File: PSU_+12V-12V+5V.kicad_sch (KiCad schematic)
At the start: 41 parts, among them J1 PSU12a, J2 PSU12b, Q1 BC557, Q2 BC557, Q3 BC547, Q4 BC547, U1 LM317L, U2 LM317L

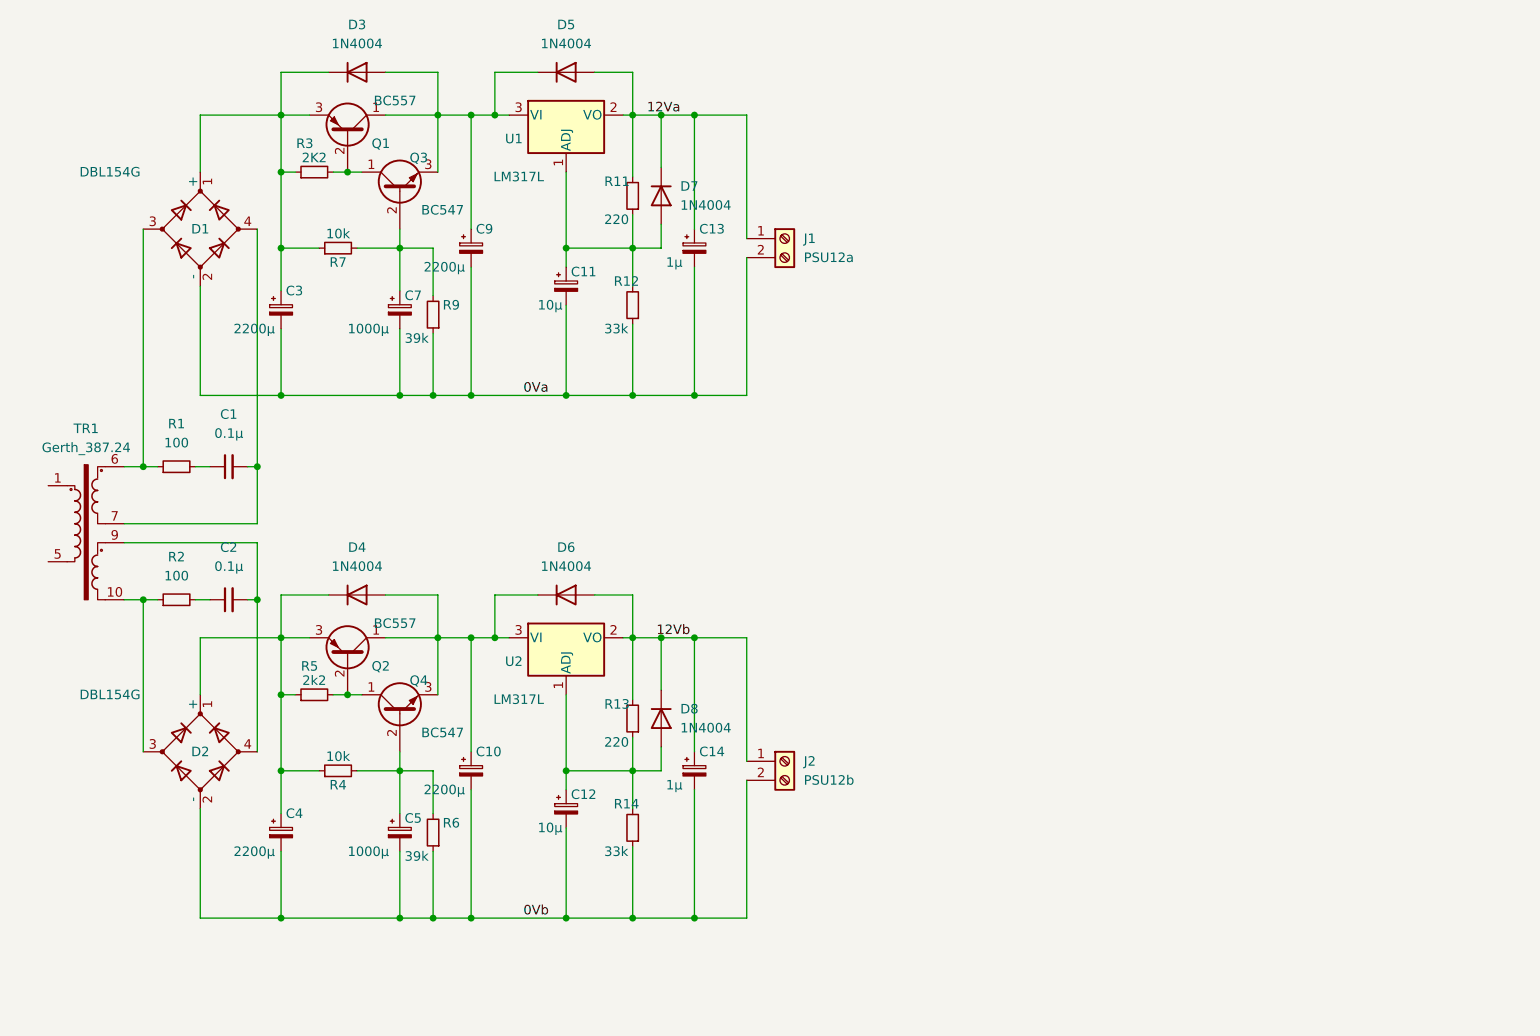
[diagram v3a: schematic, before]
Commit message: Add 5V part + 230 volt connection
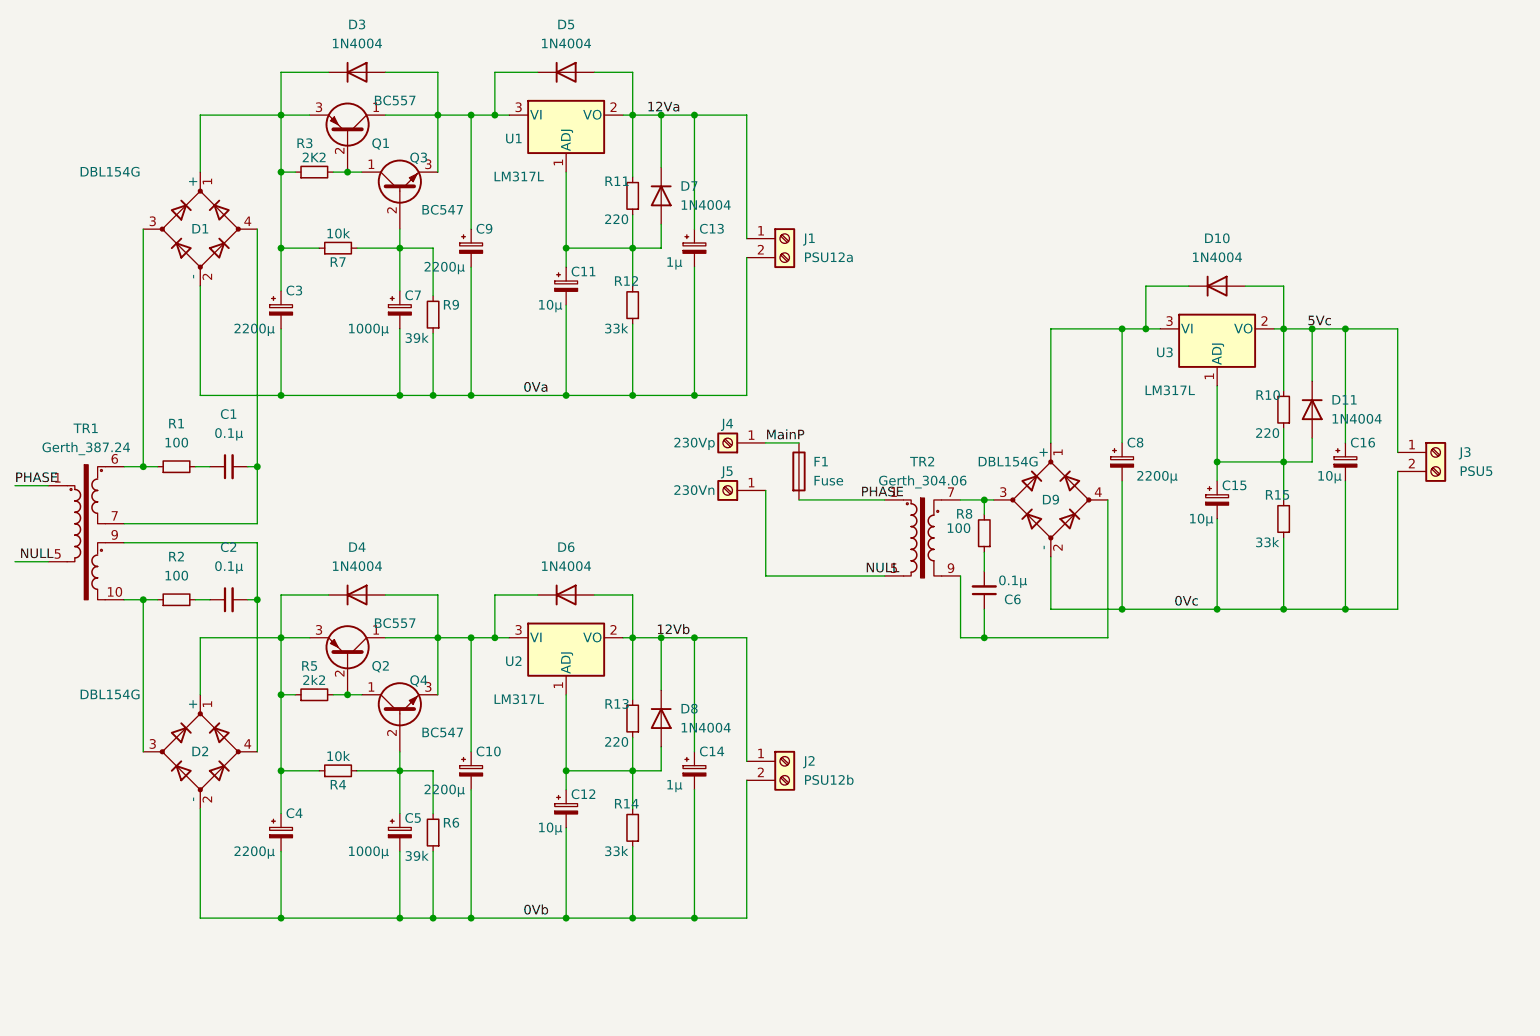
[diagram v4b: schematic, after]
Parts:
- added C15, C16: 10µ, Capacitor_THT:CP_Radial_D5.0mm_P2.50mm, symbol Device:C_Polarized_Small
- added C6: 0.1µ, Capacitor_SMD:C_1206_3216Metric_Pad1.33x1.80mm_HandSolder, symbol Device:C_Small
- added C8: 2200µ, Capacitor_THT:CP_Radial_D16.0mm_P7.50mm, symbol Device:C_Polarized_Small
- added D10, D11: 1N4004, Diode_THT:D_DO-41_SOD81_P10.16mm_Horizontal, symbol Diode:1N4004
- added D9: DBL154G, MyFootPrints:DBL_4, symbol Device:D_Bridge_+-AA
- added F1: Fuse, MyFootPrints:Fuse_Littelfuse-PTF15, symbol Device:Fuse
- added J3: PSU5, TerminalBlock_Phoenix:TerminalBlock_Phoenix_MKDS-1,5-2_1x02_P5.00mm_Horizontal, symbol Connector:Screw_Terminal_01x02
- added J4: 230Vp, TerminalBlock_MetzConnect:TerminalBlock_MetzConnect_360271_1x01_Horizontal_ScrewM3.0_Boxed, symbol Connector:Screw_Terminal_01x01
- added J5: 230Vn, TerminalBlock_MetzConnect:TerminalBlock_MetzConnect_360271_1x01_Horizontal_ScrewM3.0_Boxed, symbol Connector:Screw_Terminal_01x01
- added R10: 220, Resistor_SMD:R_1206_3216Metric_Pad1.30x1.75mm_HandSolder, symbol Device:R_Small
- added R15: 33k, Resistor_SMD:R_1206_3216Metric_Pad1.30x1.75mm_HandSolder, symbol Device:R_Small
- added R8: 100, Resistor_SMD:R_1206_3216Metric_Pad1.30x1.75mm_HandSolder, symbol Device:R_Small
- added TR2: Gerth_304.06, MyFootPrints:304.06_1.8VA, symbol Transformer:TEZ1.5-D-1
- added U3: LM317L, Package_TO_SOT_THT:TO-92_Inline_Wide, symbol Regulator_Linear:LM317L_TO92
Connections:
- net PHASE: now reaches TR1.1
- net PHASE: now also F1.2, TR2.1
- net NULL: now reaches TR1.5
- net NULL: now also J5.1 (Pin_1), TR2.5
- new net: C6.2, R8.1
- new net: D9.3, R8.2, TR2.7
- new net: C15.1, D11.2 (A), R10.1, R15.2, U3.1 (ADJ)
- new net: C8.1, D10.1 (K), D9.1 (+), U3.3 (VI)
- new net: C6.1, D9.4, TR2.9
- new net 0Vc: C15.2, C16.2, C8.2, D9.2 (-), J3.2 (Pin_2), R15.1
- new net 5Vc: C16.1, D10.2 (A), D11.1 (K), J3.1 (Pin_1), R10.2, U3.2 (VO)
- new net MainP: F1.1, J4.1 (Pin_1)

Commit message: ...
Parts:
- removed J4: 230Vp, TerminalBlock_MetzConnect:TerminalBlock_MetzConnect_360271_1x01_Horizontal_ScrewM3.0_Boxed, symbol Connector:Screw_Terminal_01x01
- removed J5: 230Vn, TerminalBlock_MetzConnect:TerminalBlock_MetzConnect_360271_1x01_Horizontal_ScrewM3.0_Boxed, symbol Connector:Screw_Terminal_01x01
- added H1, H2, H3, H4: MountingHole, MountingHole:MountingHole_3.2mm_M3, symbol Mechanical:MountingHole
- added J4: 230V, TerminalBlock_Phoenix:TerminalBlock_Phoenix_MKDS-1,5-3_1x03_P5.00mm_Horizontal, symbol Connector:Screw_Terminal_01x03
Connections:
- net MainP: now also J4.3 (Pin_3)
- net NULL: now also J4.1 (Pin_1)
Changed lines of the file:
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@@
     (stroke (width 0) (type default) (color 0 0 0 0))
   )
-  (wire (pts (xy 120.65 77.47) (xy 120.65 88.9))
+  (wire (pts (xy 120.65 76.2) (xy 120.65 88.9))
     (stroke (width 0) (type default) (color 0 0 0 0))
   )
@@
     (stroke (width 0) (type default) (color 0 0 0 0))
   )
+  (wire (pts (xy 118.11 76.2) (xy 120.65 76.2))
+    (stroke (width 0) (type default) (color 0 0 0 0))
+  )
   (wire (pts (xy 180.975 81.28) (xy 180.975 93.345))
     (stroke (width 0) (type default) (color 0 0 0 0))
@@
     (stroke (width 0) (type default) (color 0 0 0 0))
   )
-  (wire (pts (xy 120.65 71.12) (xy 125.095 71.12))
+  (wire (pts (xy 118.11 71.12) (xy 125.095 71.12))
     (stroke (width 0) (type default) (color 0 0 0 0))
   )
@@
     (pin "2")
   )
+  (symbol (lib_id "Mechanical:MountingHole") (at 154.9683 21.6637 0) (unit 1)
+    (in_bom yes) (on_board yes) (fields_autoplaced)
+    (property "Reference" "H2" (id 0) (at 157.5083 20.3936 0)
+      (effects (font (size 1.27 1.27)) (justify left))
+    )
+    (property "Value" "MountingHole" (id 1) (at 157.5083 22.9336 0)
+      (effects (font (size 1.27 1.27)) (justify left))
+    )
+    (property "Footprint" "MountingHole:MountingHole_3.2mm_M3" (id 2) (at 154.9683 21.6637 0)
+      (effects (font (size 1.27 1.27)) hide)
+    )
+    (property "Datasheet" "~" (id 3) (at 154.9683 21.6637 0)
+      (effects (font (size 1.27 1.27)) hide)
+    )
+  )
   (symbol (lib_id "Diode:1N4004") (at 106.68 107.95 270) (unit 1)
     (in_bom yes) (on_board yes) (fields_autoplaced)
@@
     (pin "1")
     (pin "2")
+  )
+  (symbol (lib_id "Mechanical:MountingHole") (at 161.29 21.59 0) (unit 1)
+    (in_bom yes) (on_board yes) (fields_autoplaced)
+    (property "Reference" "H1" (id 0) (at 163.83 20.3199 0)
+      (effects (font (size 1.27 1.27)) (justify left))
+    )
+    (property "Value" "MountingHole" (id 1) (at 163.83 22.8599 0)
+      (effects (font (size 1.27 1.27)) (justify left))
+    )
+    (property "Footprint" "MountingHole:MountingHole_3.2mm_M3" (id 2) (at 161.29 21.59 0)
+      (effects (font (size 1.27 1.27)) hide)
+    )
+    (property "Datasheet" "~" (id 3) (at 161.29 21.59 0)
+      (effects (font (size 1.27 1.27)) hide)
+    )
   )
   (symbol (lib_id "Diode:1N4004") (at 193.675 66.675 270) (unit 1)
@@
     (pin "2")
   )
-  (symbol (lib_id "Connector:Screw_Terminal_01x01") (at 115.57 77.47 180) (unit 1)
-    (in_bom yes) (on_board yes)
-    (property "Reference" "J5" (id 0) (at 115.57 74.93 0))
-    (property "Value" "230Vn" (id 1) (at 111.125 77.47 0))
-    (property "Footprint" "TerminalBlock_MetzConnect:TerminalBlock_MetzConnect_360271_1x01_Horizontal_ScrewM3.0_Boxed" (id 2) (at 115.57 77.47 0)
-      (effects (font (size 1.27 1.27)) hide)
-    )
-    (property "Datasheet" "~" (id 3) (at 115.57 77.47 0)
-      (effects (font (size 1.27 1.27)) hide)
-    )
-    (pin "1")
+  (symbol (lib_id "Mechanical:MountingHole") (at 161.7213 28.0636 0) (unit 1)
+    (in_bom yes) (on_board yes) (fields_autoplaced)
+    (property "Reference" "H4" (id 0) (at 164.2613 26.7935 0)
+      (effects (font (size 1.27 1.27)) (justify left))
+    )
+    (property "Value" "MountingHole" (id 1) (at 164.2613 29.3335 0)
+      (effects (font (size 1.27 1.27)) (justify left))
+    )
+    (property "Footprint" "MountingHole:MountingHole_3.2mm_M3" (id 2) (at 161.7213 28.0636 0)
+      (effects (font (size 1.27 1.27)) hide)
+    )
+    (property "Datasheet" "~" (id 3) (at 161.7213 28.0636 0)
+      (effects (font (size 1.27 1.27)) hide)
+    )
   )
   (symbol (lib_id "Device:R_Small") (at 41.91 74.295 90) (unit 1)
@@
     (pin "1")
     (pin "2")
+  )
+  (symbol (lib_id "Mechanical:MountingHole") (at 154.9683 28.4167 0) (unit 1)
+    (in_bom yes) (on_board yes) (fields_autoplaced)
+    (property "Reference" "H3" (id 0) (at 157.5083 27.1466 0)
+      (effects (font (size 1.27 1.27)) (justify left))
+    )
+    (property "Value" "MountingHole" (id 1) (at 157.5083 29.6866 0)
+      (effects (font (size 1.27 1.27)) (justify left))
+    )
+    (property "Footprint" "MountingHole:MountingHole_3.2mm_M3" (id 2) (at 154.9683 28.4167 0)
+      (effects (font (size 1.27 1.27)) hide)
+    )
+    (property "Datasheet" "~" (id 3) (at 154.9683 28.4167 0)
+      (effects (font (size 1.27 1.27)) hide)
+    )
   )
   (symbol (lib_id "Device:C_Small") (at 48.895 92.075 90) (unit 1)
@@
     (pin "3")
   )
-  (symbol (lib_id "Connector:Screw_Terminal_01x01") (at 115.57 71.12 180) (unit 1)
-    (in_bom yes) (on_board yes)
-    (property "Reference" "J4" (id 0) (at 115.57 68.58 0))
-    (property "Value" "230Vp" (id 1) (at 111.125 71.12 0))
-    (property "Footprint" "TerminalBlock_MetzConnect:TerminalBlock_MetzConnect_360271_1x01_Horizontal_ScrewM3.0_Boxed" (id 2) (at 115.57 71.12 0)
-      (effects (font (size 1.27 1.27)) hide)
-    )
-    (property "Datasheet" "~" (id 3) (at 115.57 71.12 0)
-      (effects (font (size 1.27 1.27)) hide)
-    )
-    (pin "1")
-  )
   (symbol (lib_id "Diode:1N4004") (at 93.98 91.44 0) (unit 1)
     (in_bom yes) (on_board yes) (fields_autoplaced)
@@
     (pin "2")
   )
+  (symbol (lib_id "Connector:Screw_Terminal_01x03") (at 113.03 73.66 180) (unit 1)
+    (in_bom yes) (on_board yes)
+    (property "Reference" "J4" (id 0) (at 113.03 64.77 0))
+    (property "Value" "230V" (id 1) (at 108.585 73.66 0))
+    (property "Footprint" "TerminalBlock_Phoenix:TerminalBlock_Phoenix_MKDS-1,5-3_1x03_P5.00mm_Horizontal" (id 2) (at 113.03 73.66 0)
+      (effects (font (size 1.27 1.27)) hide)
+    )
+    (property "Datasheet" "~" (id 3) (at 113.03 73.66 0)
+      (effects (font (size 1.27 1.27)) hide)
+    )
+    (pin "1")
+    (pin "2")
+    (pin "3")
+  )
   (sheet_instances
     (path "/" (page "1"))
@@
       (reference "F1") (unit 1) (value "Fuse") (footprint "MyFootPrints:Fuse_Littelfuse-PTF15")
     )
+    (path "/35391cf2-3cf2-436c-8d27-de8c3bcd7990"
+      (reference "H1") (unit 1) (value "MountingHole") (footprint "MountingHole:MountingHole_3.2mm_M3")
+    )
+    (path "/092f2b1b-cd5d-443d-acd1-a09235859417"
+      (reference "H2") (unit 1) (value "MountingHole") (footprint "MountingHole:MountingHole_3.2mm_M3")
+    )
+    (path "/ae12413a-2d8c-4589-95cf-ebc13663e208"
+      (reference "H3") (unit 1) (value "MountingHole") (footprint "MountingHole:MountingHole_3.2mm_M3")
+    )
+    (path "/56df0299-36cb-4393-9aeb-23633f1a391d"
+      (reference "H4") (unit 1) (value "MountingHole") (footprint "MountingHole:MountingHole_3.2mm_M3")
+    )
     (path "/267aca1d-0cf0-41ab-8780-187b83e1d640"
       (reference "J1") (unit 1) (value "PSU12a") (footprint "TerminalBlock_Phoenix:TerminalBlock_Phoenix_MKDS-1,5-2_1x02_P5.00mm_Horizontal")
@@
       (reference "J3") (unit 1) (value "PSU5") (footprint "TerminalBlock_Phoenix:TerminalBlock_Phoenix_MKDS-1,5-2_1x02_P5.00mm_Horizontal")
     )
-    (path "/d558509b-4fc8-423f-896a-7afa64c91d0c"
-      (reference "J4") (unit 1) (value "230Vp") (footprint "TerminalBlock_MetzConnect:TerminalBlock_MetzConnect_360271_1x01_Horizontal_ScrewM3.0_Boxed")
-    )
-    (path "/5a936882-5081-4041-9286-57b2f9649293"
-      (reference "J5") (unit 1) (value "230Vn") (footprint "TerminalBlock_MetzConnect:TerminalBlock_MetzConnect_360271_1x01_Horizontal_ScrewM3.0_Boxed")
+    (path "/fdb6604f-32f1-404c-8875-abfafd07f43a"
+      (reference "J4") (unit 1) (value "230V") (footprint "TerminalBlock_Phoenix:TerminalBlock_Phoenix_MKDS-1,5-3_1x03_P5.00mm_Horizontal")
     )
     (path "/961e5191-6ef0-485b-8715-bf0eec14a118"

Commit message: Changed footprint of LM317L
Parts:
- U1, U2, U3: footprint Package_TO_SOT_THT:TO-92_Inline_Wide -> MyFootPrints:LM317L_TO92
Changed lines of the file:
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@@
     (property "Reference" "U3" (id 0) (at 173.99 59.055 0))
     (property "Value" "LM317L" (id 1) (at 174.625 64.135 0))
-    (property "Footprint" "Package_TO_SOT_THT:TO-92_Inline_Wide" (id 2) (at 180.975 50.165 0)
+    (property "Footprint" "MyFootPrints:LM317L_TO92" (id 2) (at 180.975 50.165 0)
       (effects (font (size 1.27 1.27) italic) hide)
     )
@@
     (property "Reference" "U1" (id 0) (at 86.995 30.48 0))
     (property "Value" "LM317L" (id 1) (at 87.63 35.56 0))
-    (property "Footprint" "Package_TO_SOT_THT:TO-92_Inline_Wide" (id 2) (at 93.98 21.59 0)
+    (property "Footprint" "MyFootPrints:LM317L_TO92" (id 2) (at 93.98 21.59 0)
       (effects (font (size 1.27 1.27) italic) hide)
     )
@@
     (property "Reference" "U2" (id 0) (at 86.995 100.33 0))
     (property "Value" "LM317L" (id 1) (at 87.63 105.41 0))
-    (property "Footprint" "Package_TO_SOT_THT:TO-92_Inline_Wide" (id 2) (at 93.98 91.44 0)
+    (property "Footprint" "MyFootPrints:LM317L_TO92" (id 2) (at 93.98 91.44 0)
       (effects (font (size 1.27 1.27) italic) hide)
     )
@@
     )
     (path "/d474219a-a247-4920-81cf-497b42b24261"
-      (reference "U1") (unit 1) (value "LM317L") (footprint "Package_TO_SOT_THT:TO-92_Inline_Wide")
+      (reference "U1") (unit 1) (value "LM317L") (footprint "MyFootPrints:LM317L_TO92")
     )
     (path "/fa9812ec-6ebd-43d9-915e-d9ff60029873"
-      (reference "U2") (unit 1) (value "LM317L") (footprint "Package_TO_SOT_THT:TO-92_Inline_Wide")
+      (reference "U2") (unit 1) (value "LM317L") (footprint "MyFootPrints:LM317L_TO92")
     )
     (path "/d0a35f2e-9e20-47b8-8efa-57688d169a50"
-      (reference "U3") (unit 1) (value "LM317L") (footprint "Package_TO_SOT_THT:TO-92_Inline_Wide")
-    )
-  )
+      (reference "U3") (unit 1) (value "LM317L") (footprint "MyFootPrints:LM317L_TO92")
+    )
+  )

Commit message: Aanpassing ijkweerstand 5V
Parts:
- added R16: 560, Resistor_SMD:R_1206_3216Metric_Pad1.30x1.75mm_HandSolder, symbol Device:R_Small
- R15: value 33k -> 100
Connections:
- net at C15.1, D11.2 (A), R10.1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: now also R16.2; no longer R15.2
- new net: R15.2, R16.1
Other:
- moved on the sheet: R15

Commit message: Changed type capacitor
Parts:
- C1, C2, C6: footprint Capacitor_SMD:C_1206_3216Metric_Pad1.33x1.80mm_HandSolder -> Capacitor_THT:C_Disc_D6.0mm_W2.5mm_P5.00mm
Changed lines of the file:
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@@
     (property "Reference" "C1" (id 0) (at 48.9013 67.31 90))
     (property "Value" "0.1µ" (id 1) (at 48.9013 69.85 90))
-    (property "Footprint" "Capacitor_SMD:C_1206_3216Metric_Pad1.33x1.80mm_HandSolder" (id 2) (at 48.895 74.295 0)
+    (property "Footprint" "Capacitor_THT:C_Disc_D6.0mm_W2.5mm_P5.00mm" (id 2) (at 48.895 74.295 0)
       (effects (font (size 1.27 1.27)) hide)
     )
@@
     (property "Reference" "C6" (id 0) (at 153.67 92.075 0))
     (property "Value" "0.1µ" (id 1) (at 153.67 89.535 0))
-    (property "Footprint" "Capacitor_SMD:C_1206_3216Metric_Pad1.33x1.80mm_HandSolder" (id 2) (at 149.86 90.805 0)
+    (property "Footprint" "Capacitor_THT:C_Disc_D6.0mm_W2.5mm_P5.00mm" (id 2) (at 149.86 90.805 0)
       (effects (font (size 1.27 1.27)) hide)
     )
@@
     (property "Reference" "C2" (id 0) (at 48.9013 85.09 90))
     (property "Value" "0.1µ" (id 1) (at 48.9013 87.63 90))
-    (property "Footprint" "Capacitor_SMD:C_1206_3216Metric_Pad1.33x1.80mm_HandSolder" (id 2) (at 48.895 92.075 0)
+    (property "Footprint" "Capacitor_THT:C_Disc_D6.0mm_W2.5mm_P5.00mm" (id 2) (at 48.895 92.075 0)
       (effects (font (size 1.27 1.27)) hide)
     )
@@
   (symbol_instances
     (path "/6fd7016a-1730-40c6-9d0e-a95a44381179"
-      (reference "C1") (unit 1) (value "0.1µ") (footprint "Capacitor_SMD:C_1206_3216Metric_Pad1.33x1.80mm_HandSolder")
+      (reference "C1") (unit 1) (value "0.1µ") (footprint "Capacitor_THT:C_Disc_D6.0mm_W2.5mm_P5.00mm")
     )
     (path "/b293b6b5-17ee-4dd0-9c2c-4292fce38419"
-      (reference "C2") (unit 1) (value "0.1µ") (footprint "Capacitor_SMD:C_1206_3216Metric_Pad1.33x1.80mm_HandSolder")
+      (reference "C2") (unit 1) (value "0.1µ") (footprint "Capacitor_THT:C_Disc_D6.0mm_W2.5mm_P5.00mm")
     )
     (path "/a4d6fd72-18d2-4035-a3c8-20337a49b6b9"
@@
     )
     (path "/97520acb-35f8-48c3-a00c-f4b323cc3ab9"
-      (reference "C6") (unit 1) (value "0.1µ") (footprint "Capacitor_SMD:C_1206_3216Metric_Pad1.33x1.80mm_HandSolder")
+      (reference "C6") (unit 1) (value "0.1µ") (footprint "Capacitor_THT:C_Disc_D6.0mm_W2.5mm_P5.00mm")
     )
     (path "/c1f10308-ec7f-47d2-9f01-fc99bc203e3f"
